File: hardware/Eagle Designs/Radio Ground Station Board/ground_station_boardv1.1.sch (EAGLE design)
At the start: 3 parts, among them U1 RFM23BP

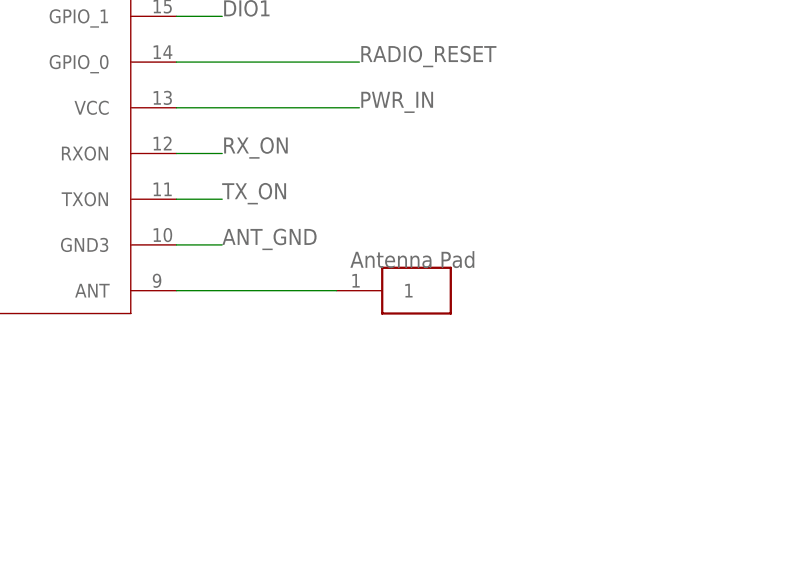
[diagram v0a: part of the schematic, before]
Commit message: Swapped the antenna pad for the MCX connector on the ground station board. Created the mock transmission board which is a radio, teensy and antenna.
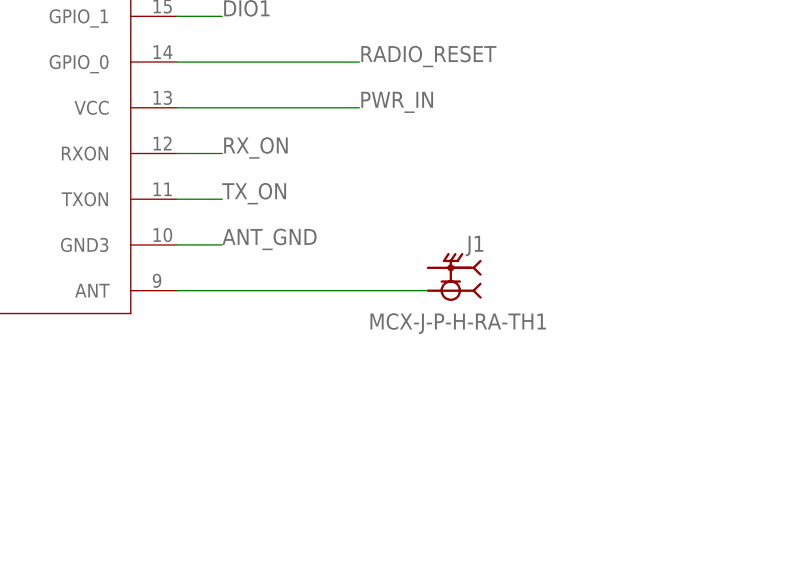
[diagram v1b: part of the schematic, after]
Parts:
- removed U$2: ANTENNA_PAD+HOLES, Antenna_Pad:ANTENNA_PAD+HOLES
- added J1: MCX-J-P-H-RA-TH1, OBCv4:MCX-J-P-H-RA-TH1
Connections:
- net N$1: now also J1.1; no longer U$2.1
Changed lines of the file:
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@@
 <part name="U$1" library="OBCv4" deviceset="TEENSY41" device="TEENSY"/>
 <part name="U1" library="RFM RADIOS" deviceset="RFM23BP" device=""/>
-<part name="U$2" library="Antenna_Pad" deviceset="ANTENNA_PAD+HOLES" device=""/>
+<part name="J1" library="OBCv4" deviceset="MCX-J-P-H-RA-TH1" device=""/>
 </parts>
 <sheets>
@@
 <attribute name="VALUE" x="264.16" y="152.908" size="1.778" layer="96"/>
 </instance>
-<instance part="U$2" gate="G$1" x="320.04" y="154.94" smashed="yes"/>
+<instance part="J1" gate="G$1" x="327.66" y="160.02" smashed="yes" rot="R180">
+<attribute name="NAME" x="331.47" y="163.576" size="1.778" layer="95" rot="R180"/>
+<attribute name="VALUE" x="318.516" y="153.162" size="1.778" layer="96"/>
+</instance>
 </instances>
 <busses>
@@
 <net name="N$1" class="0">
 <segment>
-<pinref part="U$2" gate="G$1" pin="1"/>
+<pinref part="J1" gate="G$1" pin="1"/>
 <pinref part="U1" gate="G$1" pin="ANT"/>
-<wire x1="314.96" y1="157.48" x2="297.18" y2="157.48" width="0.1524" layer="91"/>
-</segment>
-</net>
+<wire x1="325.12" y1="157.48" x2="297.18" y2="157.48" width="0.1524" layer="91"/>
+</segment>
+</net>

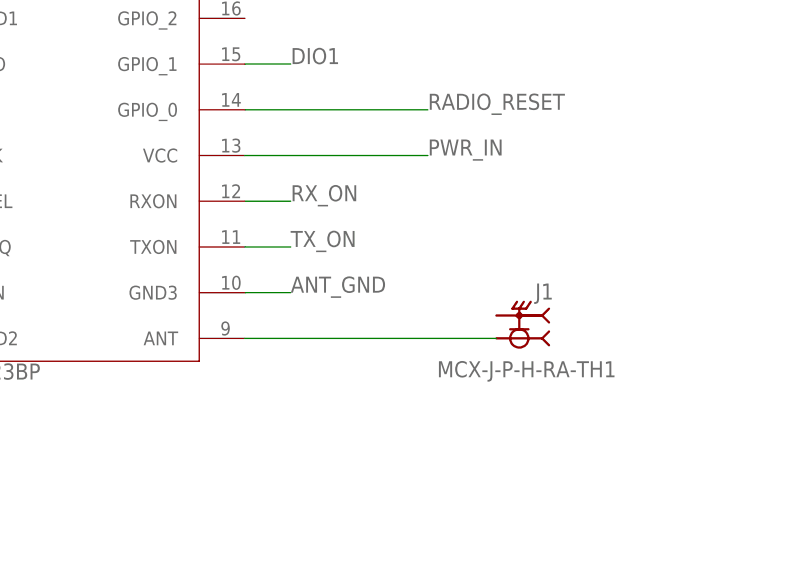
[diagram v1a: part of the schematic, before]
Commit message: Added RF ground plane to ground station board.
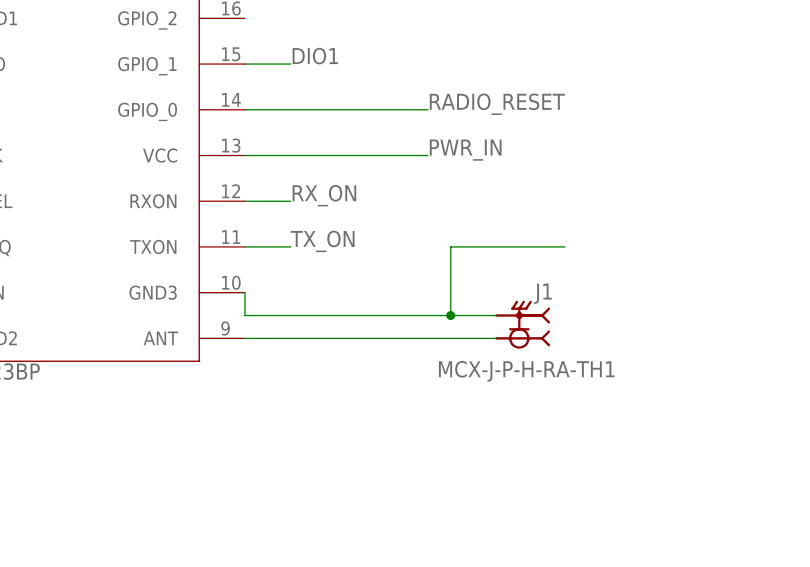
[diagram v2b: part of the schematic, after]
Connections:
- removed net ANT_GND: U1.GND3
- new net RF_GND: J1.2, U1.GND3
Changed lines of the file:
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@@
-</segment>
-</net>
-<net name="ANT_GND" class="0">
-<segment>
-<pinref part="U1" gate="G$1" pin="GND3"/>
-<wire x1="297.18" y1="162.56" x2="302.26" y2="162.56" width="0.1524" layer="91"/>
-<label x="302.26" y="162.56" size="1.778" layer="95"/>
 </segment>
 </net>
@@
 </segment>
 </net>
+<net name="RF_GND" class="0">
+<segment>
+<pinref part="J1" gate="G$1" pin="2"/>
+<pinref part="U1" gate="G$1" pin="GND3"/>
+<wire x1="325.12" y1="160.02" x2="320.04" y2="160.02" width="0.1524" layer="91"/>
+<wire x1="320.04" y1="160.02" x2="297.18" y2="160.02" width="0.1524" layer="91"/>
+<wire x1="297.18" y1="160.02" x2="297.18" y2="162.56" width="0.1524" layer="91"/>
+<wire x1="320.04" y1="160.02" x2="320.04" y2="167.64" width="0.1524" layer="91"/>
+<wire x1="320.04" y1="167.64" x2="332.74" y2="167.64" width="0.1524" layer="91"/>
+<junction x="320.04" y="160.02"/>
+</segment>
+</net>

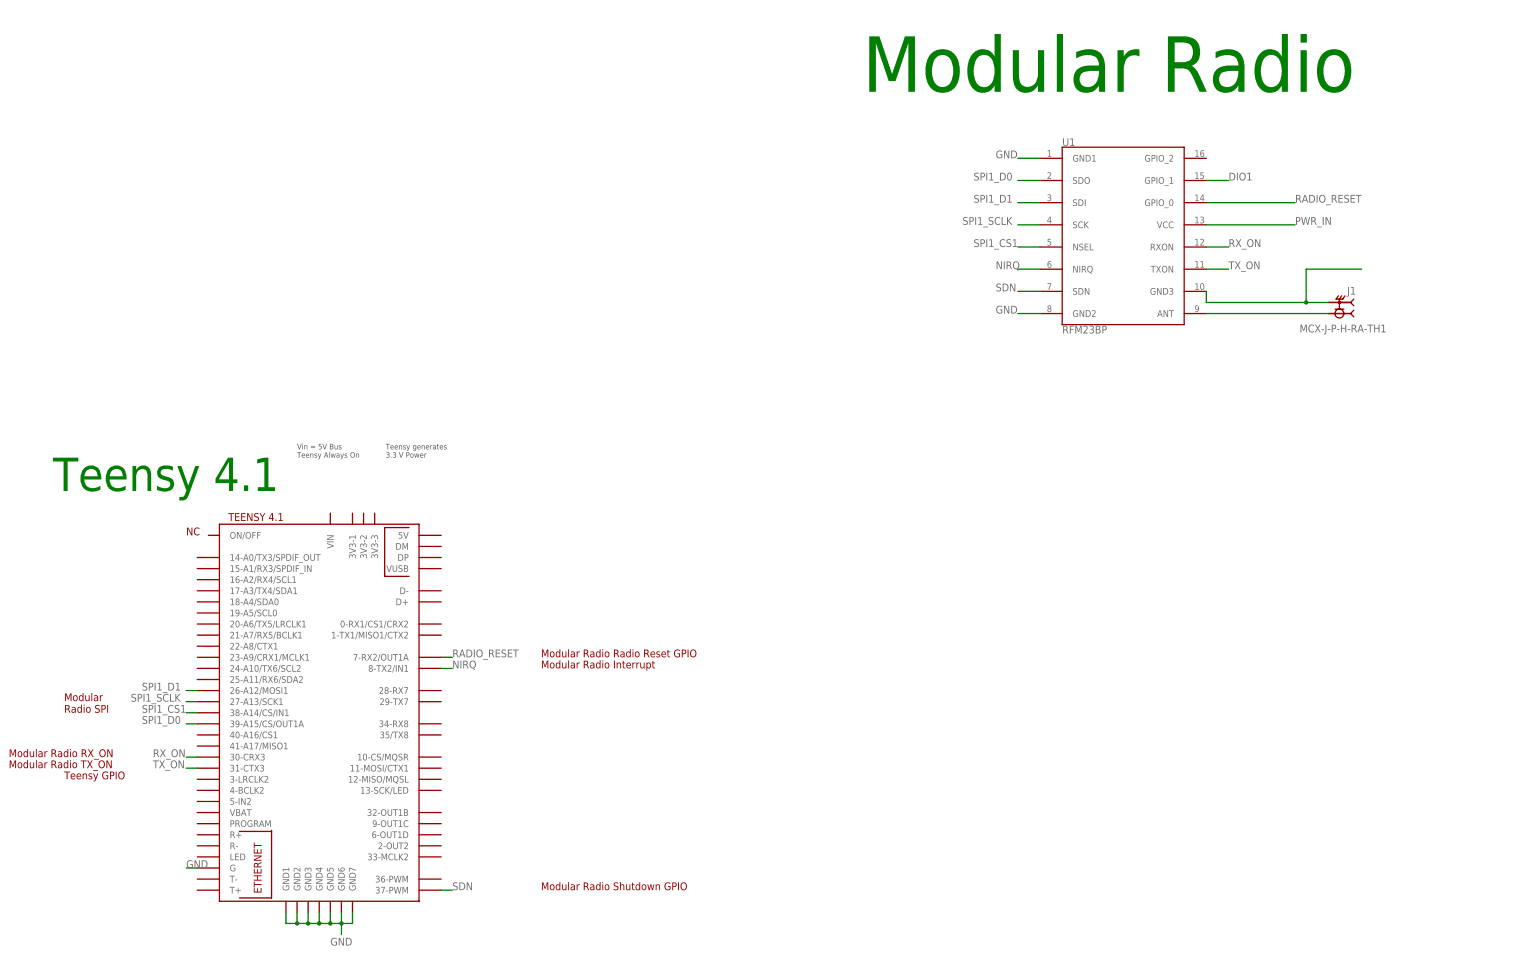
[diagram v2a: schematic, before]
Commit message: Modified pin configuration on the ground station board to match OBC 4.24.
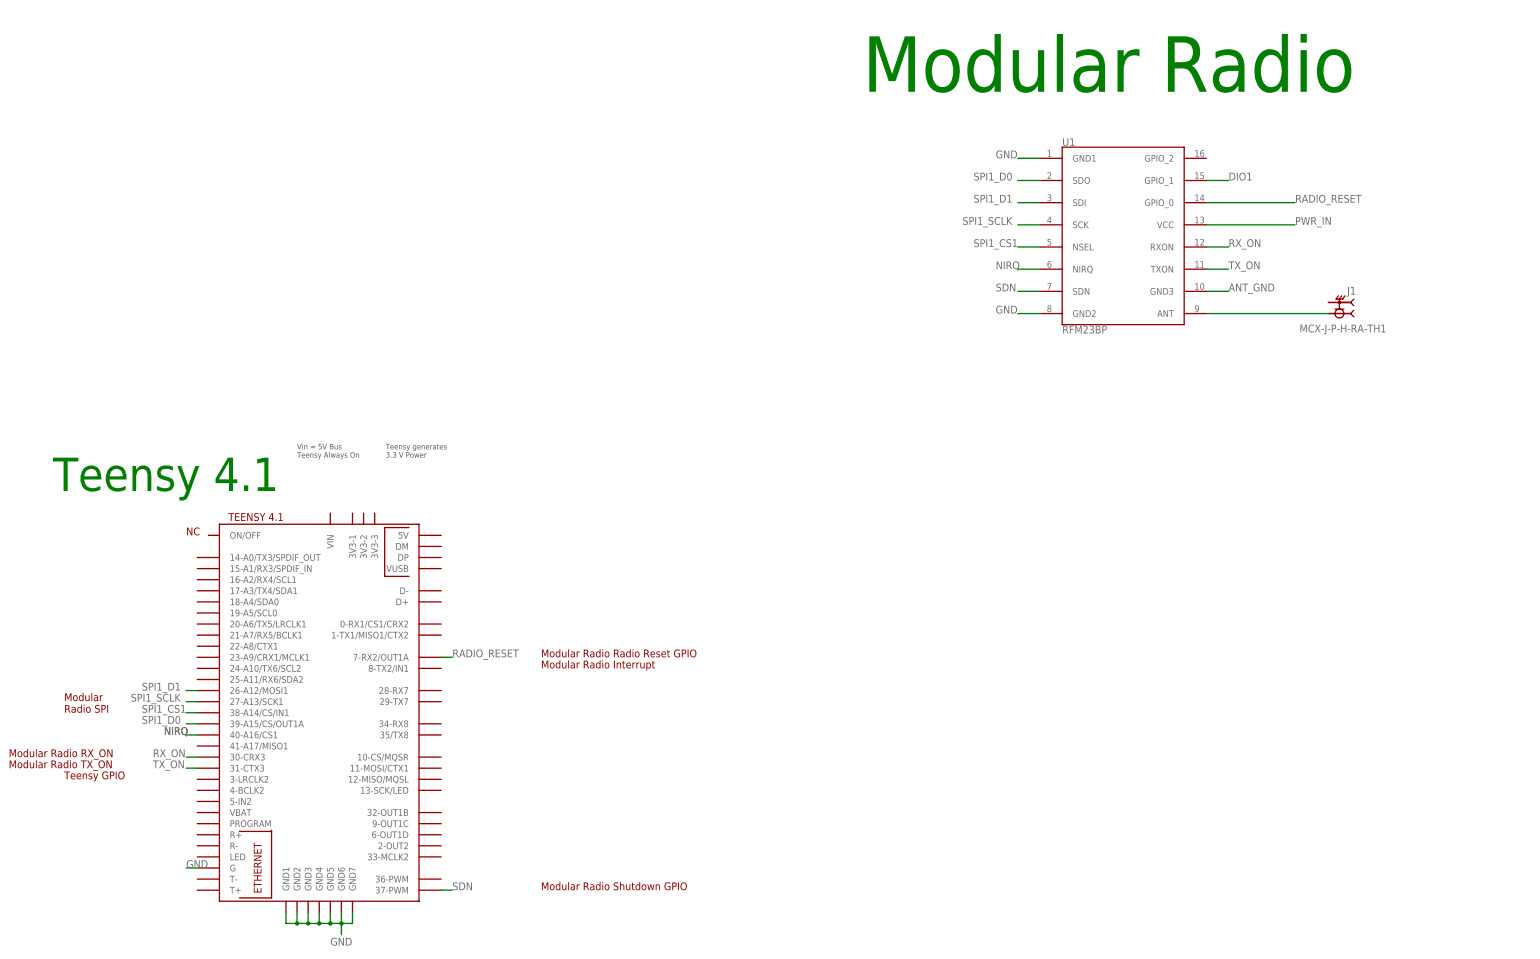
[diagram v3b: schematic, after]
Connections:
- removed net RF_GND: J1.2, U1.GND3
- new net ANT_GND: U1.GND3
- net NIRQ: now also U$1.40-A16/CS1; no longer U$1.8-TX2/IN1
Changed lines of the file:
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@@
 <net name="NIRQ" class="0">
-<segment>
-<pinref part="U$1" gate="G$1" pin="8-TX2/IN1"/>
-<wire x1="121.92" y1="76.2" x2="124.46" y2="76.2" width="0.1524" layer="91"/>
-<label x="124.46" y="76.2" size="1.778" layer="95"/>
-</segment>
 <segment>
 <pinref part="U1" gate="G$1" pin="NIRQ"/>
 <wire x1="259.08" y1="167.64" x2="254" y2="167.64" width="0.1524" layer="91"/>
 <label x="248.92" y="167.64" size="1.778" layer="95"/>
+</segment>
+<segment>
+<pinref part="U$1" gate="G$1" pin="40-A16/CS1"/>
+<wire x1="66.04" y1="60.96" x2="63.5" y2="60.96" width="0.1524" layer="91"/>
+<label x="58.42" y="60.96" size="1.778" layer="95"/>
+<label x="58.42" y="60.96" size="1.778" layer="95"/>
 </segment>
 </net>
@@
 <wire x1="297.18" y1="187.96" x2="302.26" y2="187.96" width="0.1524" layer="91"/>
 <label x="302.26" y="187.96" size="1.778" layer="95"/>
+</segment>
+</net>
+<net name="ANT_GND" class="0">
+<segment>
+<pinref part="U1" gate="G$1" pin="GND3"/>
+<wire x1="297.18" y1="162.56" x2="302.26" y2="162.56" width="0.1524" layer="91"/>
+<label x="302.26" y="162.56" size="1.778" layer="95"/>
 </segment>
 </net>
@@
 </segment>
 </net>
-<net name="RF_GND" class="0">
-<segment>
-<pinref part="J1" gate="G$1" pin="2"/>
-<pinref part="U1" gate="G$1" pin="GND3"/>
-<wire x1="325.12" y1="160.02" x2="320.04" y2="160.02" width="0.1524" layer="91"/>
-<wire x1="320.04" y1="160.02" x2="297.18" y2="160.02" width="0.1524" layer="91"/>
-<wire x1="297.18" y1="160.02" x2="297.18" y2="162.56" width="0.1524" layer="91"/>
-<wire x1="320.04" y1="160.02" x2="320.04" y2="167.64" width="0.1524" layer="91"/>
-<wire x1="320.04" y1="167.64" x2="332.74" y2="167.64" width="0.1524" layer="91"/>
-<junction x="320.04" y="160.02"/>
-</segment>
-</net>

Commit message: Fixed RF ground station board... again.
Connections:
- removed net ANT_GND: U1.GND3
- new net RF_GND: J1.2, U1.GND3
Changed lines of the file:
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@@
 </segment>
 </net>
-<net name="ANT_GND" class="0">
+<net name="RF_GND" class="0">
 <segment>
 <pinref part="U1" gate="G$1" pin="GND3"/>
 <wire x1="297.18" y1="162.56" x2="302.26" y2="162.56" width="0.1524" layer="91"/>
 <label x="302.26" y="162.56" size="1.778" layer="95"/>
+<pinref part="J1" gate="G$1" pin="2"/>
+<wire x1="325.12" y1="160.02" x2="302.26" y2="160.02" width="0.1524" layer="91"/>
+<wire x1="302.26" y1="160.02" x2="302.26" y2="162.56" width="0.1524" layer="91"/>
 </segment>
 </net>
